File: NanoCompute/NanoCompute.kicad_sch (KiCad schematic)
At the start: 5 parts

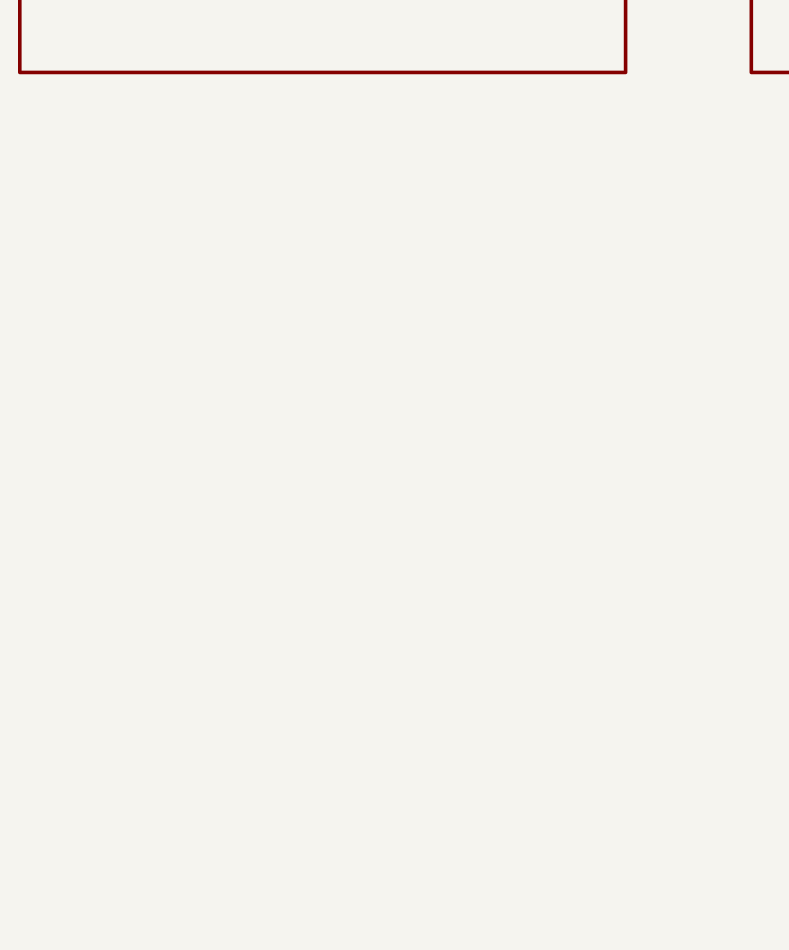
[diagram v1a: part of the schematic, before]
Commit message: Added 2 HDMI 2.1 connectors
Will delay working on any kind of power system since I'm still figuring
out what I will have on this board. Would prefer to have a PMIC than
bunch of DC-DC regulators.
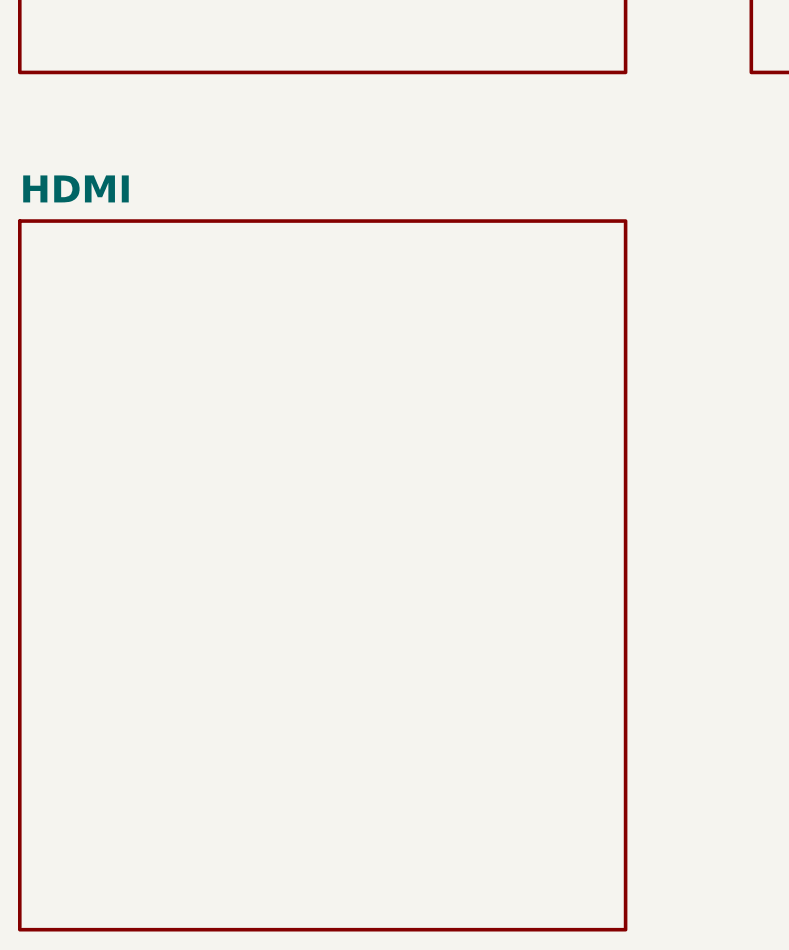
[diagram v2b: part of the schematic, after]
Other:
- added sheet HDMI (HDMI.kicad_sch)
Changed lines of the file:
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@@
+	)
+	(sheet
+		(at 24.13 120.65)
+		(size 67.31 78.74)
+		(fields_autoplaced yes)
+		(stroke
+			(width 0.4)
+			(type solid)
+			(color 0 0 0 1)
+		)
+		(fill
+			(color 74 190 97 1.0000)
+		)
+		(property "Sheetname" "HDMI"
+			(at 24.13 118.9496 0)
+			(effects
+				(font
+					(size 3 3)
+					(thickness 0.6)
+					(bold yes)
+				)
+				(justify left bottom)
+			)
+		)
+		(property "Sheetfile" "HDMI.kicad_sch"
+			(at 24.13 200.0984 0)
+			(effects
+				(font
+					(size 1.27 1.27)
+				)
+				(justify left top)
+				(hide yes)
+			)
+		)
+		(instances
+			(project "NanoCompute"
+				(path "/3a0a6fc3-d957-4804-b3c3-6d269c038b1f"
+					(page "5")
+				)
+			)
+		)
 	)
 	(sheet

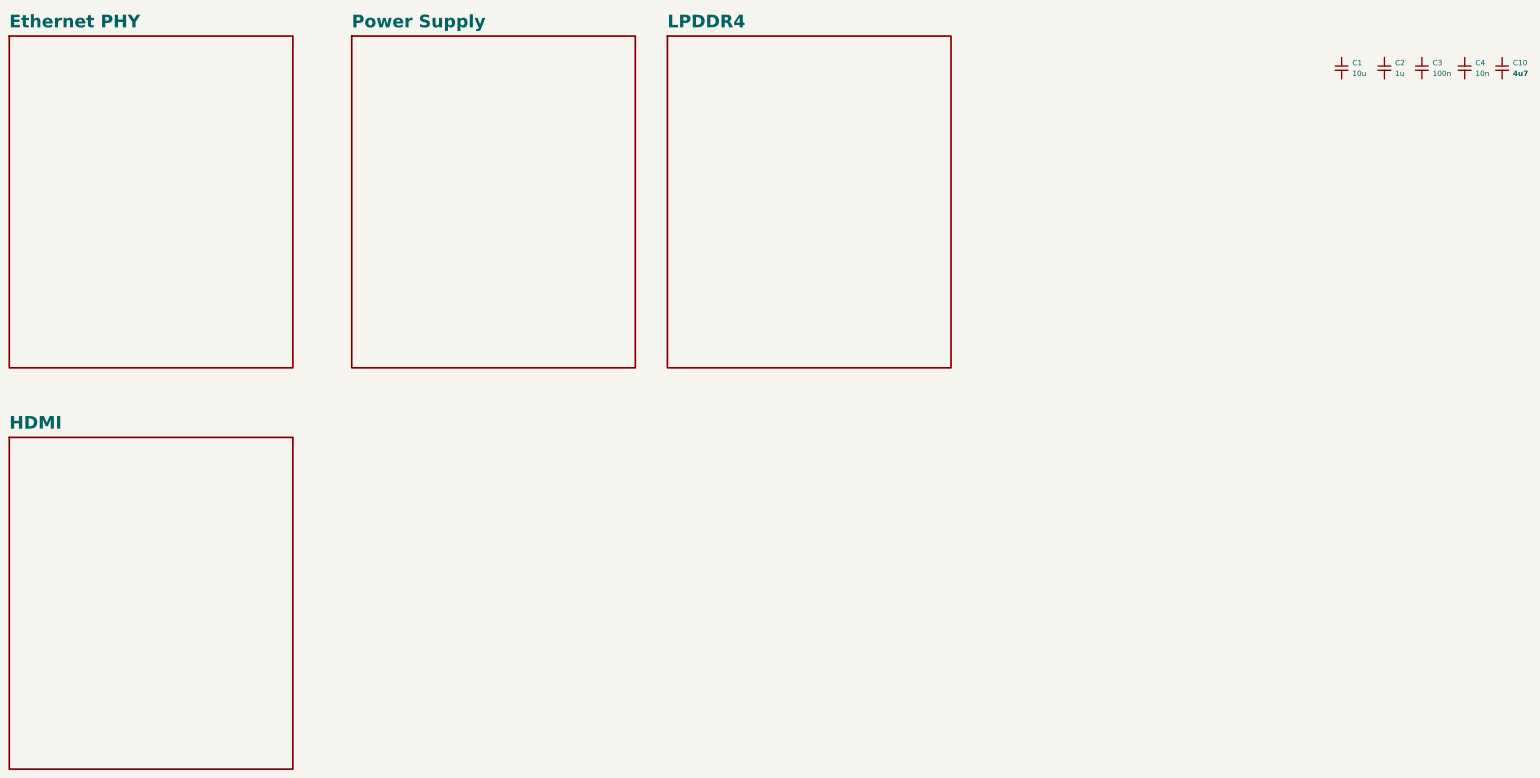
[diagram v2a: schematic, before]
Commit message: Added eMMC 5.1 HS400 128GB
It would act as a on-board primary storage while NVMe would act as an
extension/upgrade.
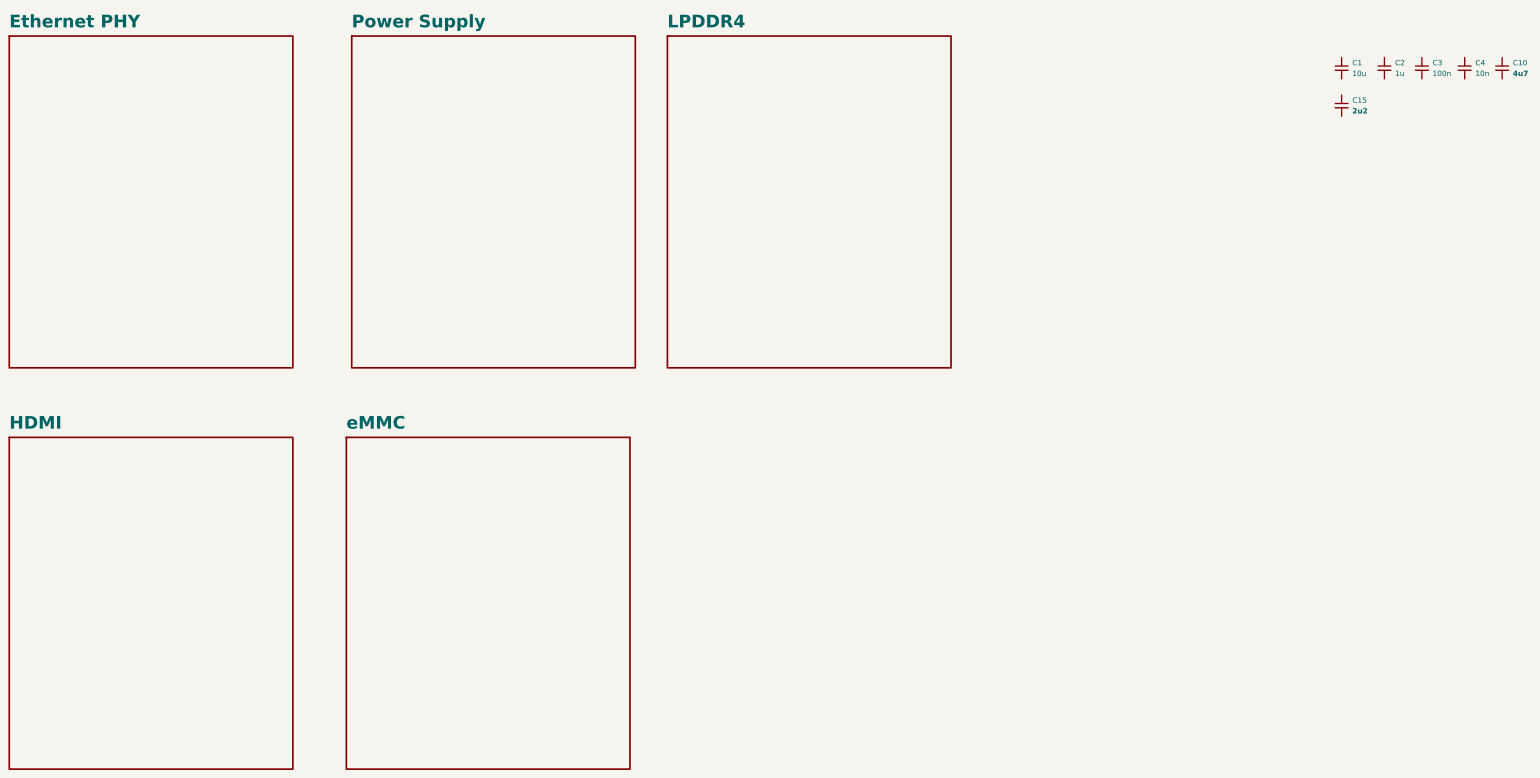
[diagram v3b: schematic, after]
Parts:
- added C15: 2u2, Capacitor_SMD:C_0201_0603Metric, symbol Device:C_Small
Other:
- added sheet eMMC (EMMC.kicad_sch)
- title: (none) -> NanoCompute
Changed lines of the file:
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@@
 	(paper "A3")
 	(title_block
-		(date "2025-01-01")
+		(title "NanoCompute")
+		(date "2025-01-06")
 		(rev "v1.0")
 	)
@@
 	(symbol
 		(lib_id "Device:C_Small")
+		(at 340.36 41.91 0)
+		(unit 1)
+		(exclude_from_sim no)
+		(in_bom yes)
+		(on_board yes)
+		(dnp no)
+		(fields_autoplaced yes)
+		(property "Reference" "C15"
+			(at 342.9 40.6462 0)
+			(effects
+				(font
+					(size 1.27 1.27)
+				)
+				(justify left)
+			)
+		)
+		(property "Value" "2u2"
+			(at 342.9 43.1862 0)
+			(effects
+				(font
+					(size 1.27 1.27)
+					(thickness 0.254)
+					(bold yes)
+				)
+				(justify left)
+			)
+		)
+		(property "Footprint" "Capacitor_SMD:C_0201_0603Metric"
+			(at 340.36 41.91 0)
+			(effects
+				(font
+					(size 1.27 1.27)
+				)
+				(hide yes)
+			)
+		)
+		(property "Datasheet" "https://search.murata.co.jp/Ceramy/image/img/A01X/G101/ENG/GRM033R60J225ME47-01.pdf"
+			(at 340.36 41.91 0)
+			(effects
+				(font
+					(size 1.27 1.27)
+				)
+				(hide yes)
+			)
+		)
+		(property "Description" "2.2 µF ±20% 6.3V Ceramic Capacitor X5R 0201 (0603 Metric)"
+			(at 340.36 41.91 0)
+			(effects
+				(font
+					(size 1.27 1.27)
+				)
+				(hide yes)
+			)
+		)
+		(property "Digikey stock" "7,591,739 - 6/7/2024"
+			(at 340.36 41.91 0)
+			(effects
+				(font
+					(size 1.27 1.27)
+				)
+				(hide yes)
+			)
+		)
+		(property "MPN" "GRM033R60J225ME47D"
+			(at 340.36 41.91 0)
+			(effects
+				(font
+					(size 1.27 1.27)
+				)
+				(hide yes)
+			)
+		)
+		(pin "1"
+		)
+		(pin "2"
+		)
+		(instances
+			(project "NanoCompute"
+				(path "/3a0a6fc3-d957-4804-b3c3-6d269c038b1f"
+					(reference "C15")
+					(unit 1)
+				)
+			)
+		)
+	)
+	(symbol
+		(lib_id "Device:C_Small")
 		(at 340.36 33.02 0)
 		(unit 1)
@@
 				)
 			)
+		)
+	)
+	(sheet
+		(at 104.14 120.65)
+		(size 67.31 78.74)
+		(fields_autoplaced yes)
+		(stroke
+			(width 0.4)
+			(type solid)
+			(color 0 0 0 1)
+		)
+		(fill
+			(color 74 190 97 1.0000)
+		)
+		(property "Sheetname" "eMMC"
+			(at 104.14 118.9496 0)
+			(effects
+				(font
+					(size 3 3)
+					(thickness 0.6)
+					(bold yes)
+				)
+				(justify left bottom)
+			)
+		)
+		(property "Sheetfile" "EMMC.kicad_sch"
+			(at 104.14 200.0984 0)
+			(effects
+				(font
+					(size 1.27 1.27)
+				)
+				(justify left top)
+				(hide yes)
+			)
+		)
+		(instances
+			(project "NanoCompute"
+				(path "/3a0a6fc3-d957-4804-b3c3-6d269c038b1f"
+					(page "6")
+				)
+			)
